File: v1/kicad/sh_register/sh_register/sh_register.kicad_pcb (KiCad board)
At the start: 2 copper layers, 101 x 61.5 mm, 5 parts, among them J1 OP_{out}, U1 74LS194, U2 74LS194, U3 74LS245, U4 LNCPU Type B Connector

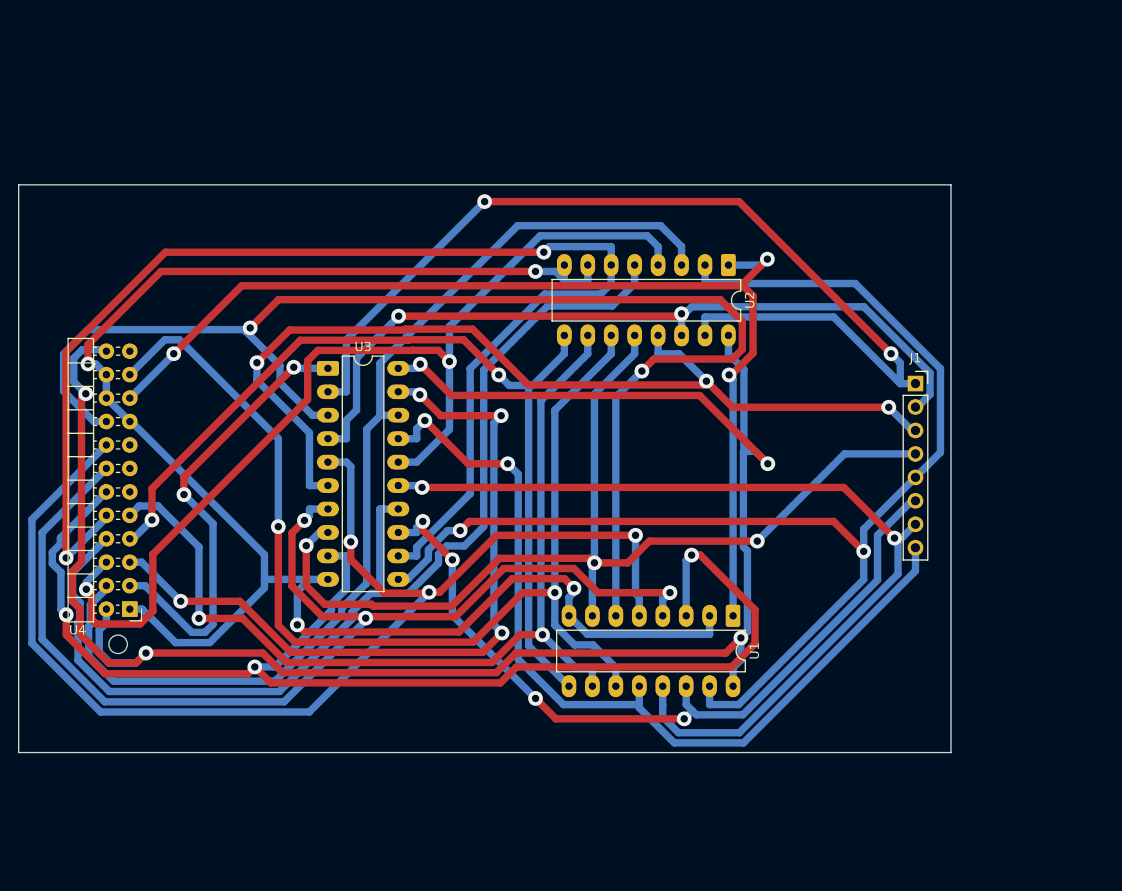
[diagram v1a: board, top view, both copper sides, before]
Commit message: check designs for ALU (partial), SP, Shift register, register
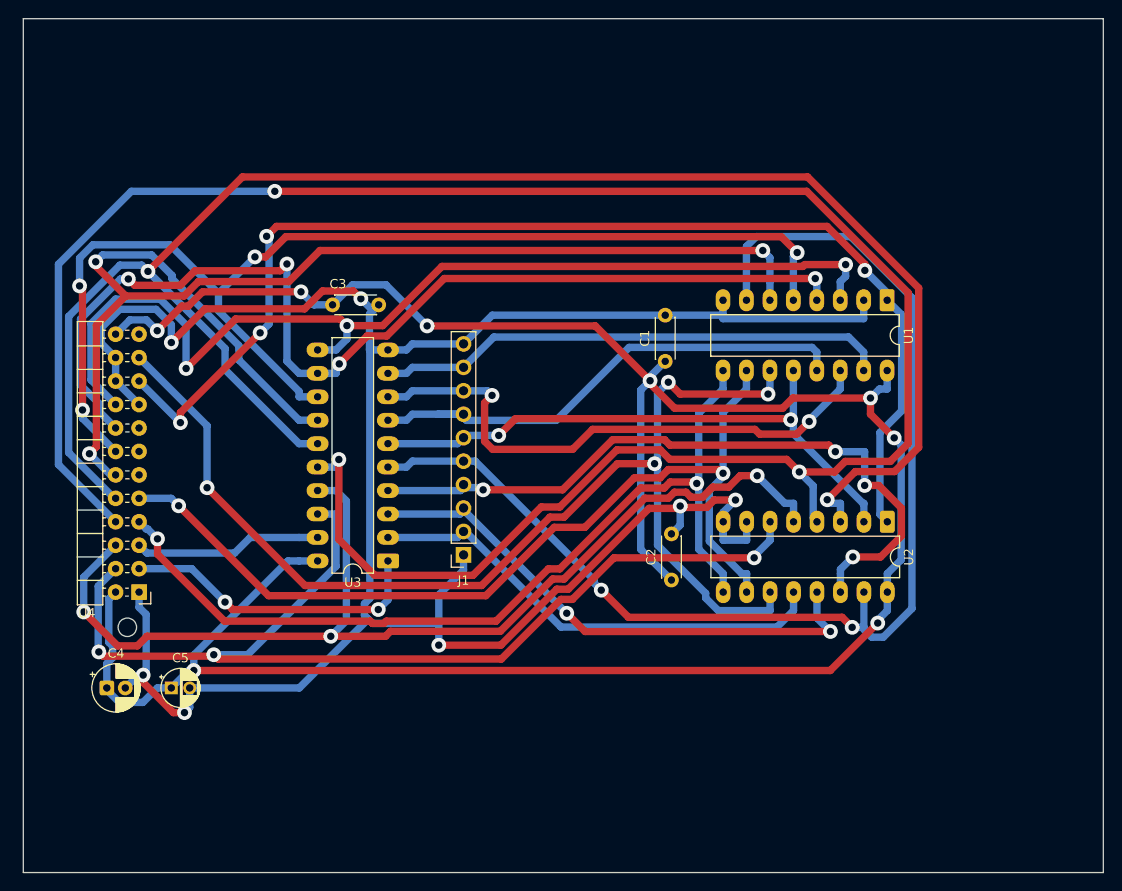
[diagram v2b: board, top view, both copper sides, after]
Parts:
- added C1: 100n, Capacitor_THT:C_Disc_D4.3mm_W1.9mm_P5.00mm, F.Cu at (132.0, 65.6)
- added C2: 100n, Capacitor_THT:C_Disc_D4.3mm_W1.9mm_P5.00mm, F.Cu at (132.7, 89.3)
- added C3: 220n, Capacitor_THT:C_Disc_D4.3mm_W1.9mm_P5.00mm, F.Cu at (96.0, 59.5)
- added C4: 47uF, Capacitor_THT:CP_Radial_D5.0mm_P2.00mm, F.Cu at (71.5, 101.0)
- added C5: 1uF, lncpu:CP_Radial_D4.0mm_P2.00mm-Large-Holes, F.Cu at (78.5, 101.0)
- J1: footprint Connector_PinSocket_2.54mm:PinSocket_1x08_P2.54mm_Vertical -> Connector_PinSocket_2.54mm:PinSocket_1x10_P2.54mm_Vertical
- U3: value 74LS245 -> 74HCT541
- U4: value LNCPU Type B Connector -> LNCPU Type B Header
- moved J1 52.4 mm to (110.2, 86.6), turned to 180 degrees
- moved U1 38.0 mm to (156.1, 59.0)
- moved U2 32.7 mm to (156.1, 83.0)
- moved U3 21.8 mm to (102.0, 87.2), turned to 180 degrees
- moved U4 2.10 mm to (75.0, 90.6)
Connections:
- J1 pad 1: /ASYNC_{out}0 -> Net-(U1-Dsr)
- J1 pad 2: /ASYNC_{out}1 -> /ASYNC_{out}0
- J1 pad 3: /ASYNC_{out}2 -> /ASYNC_{out}1
- J1 pad 4: /ASYNC_{out}3 -> /ASYNC_{out}2
- J1 pad 5: /ASYNC_{out}4 -> /ASYNC_{out}3
- J1 pad 6: /ASYNC_{out}5 -> /ASYNC_{out}4
- J1 pad 7: /ASYNC_{out}6 -> /ASYNC_{out}5
- J1 pad 8: /ASYNC_{out}7 -> /ASYNC_{out}6
- U1 pad 12: /ASYNC_{out}7 -> /ASYNC_{out}4
- U1 pad 13: /ASYNC_{out}6 -> /ASYNC_{out}5
- U1 pad 14: /ASYNC_{out}5 -> /ASYNC_{out}6
- U1 pad 15: /ASYNC_{out}4 -> /ASYNC_{out}7
- U1 pad 3: /DBUS4 -> /DBUS7
- U1 pad 4: /DBUS5 -> /DBUS6
- U1 pad 5: /DBUS6 -> /DBUS5
- U1 pad 6: /DBUS7 -> /DBUS4
- U2 pad 12: /ASYNC_{out}3 -> /ASYNC_{out}0
- U2 pad 13: /ASYNC_{out}2 -> /ASYNC_{out}1
- U2 pad 14: /ASYNC_{out}1 -> /ASYNC_{out}2
- U2 pad 15: /ASYNC_{out}0 -> /ASYNC_{out}3
- U2 pad 3: /DBUS0 -> /DBUS3
- U2 pad 4: /DBUS1 -> /DBUS2
- U2 pad 5: /DBUS2 -> /DBUS1
- U2 pad 6: /DBUS3 -> /DBUS0
- U3 pad 11: /ASYNC_{out}4 -> /DBUS7
- U3 pad 12: /DBUS3 -> /DBUS6
- U3 pad 13: /ASYNC_{out}5 -> /DBUS5
- U3 pad 14: /DBUS2 -> /DBUS4
- U3 pad 15: /ASYNC_{out}6 -> /DBUS3
- U3 pad 16: /DBUS1 -> /DBUS2
- U3 pad 17: /ASYNC_{out}7 -> /DBUS1
- U3 pad 3: /DBUS7 -> /ASYNC_{out}1
- U3 pad 4: /ASYNC_{out}1 -> /ASYNC_{out}2
- U3 pad 5: /DBUS6 -> /ASYNC_{out}3
- U3 pad 6: /ASYNC_{out}2 -> /ASYNC_{out}4
- U3 pad 7: /DBUS5 -> /ASYNC_{out}5
- U3 pad 8: /ASYNC_{out}3 -> /ASYNC_{out}6
- U3 pad 9: /DBUS4 -> /ASYNC_{out}7
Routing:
- net /DBUS2: track 119.2 -> 235.7 mm, vias 0 -> 3
- net Net-(U1-Dsr): track 181.8 -> 254.4 mm, vias 4 -> 7
- net /ASYNC_{out}4: track 136.8 -> 64.7 mm
- net Net-(U3-2OE): track 82.5 -> 20.4 mm, vias 4 -> 0
- net /ASYNC_{out}0: track 111.1 -> 51.2 mm, vias 2 -> 0
- net Net-(U1-VCC): track 209.5 -> 267.8 mm, vias 5 -> 8
- net /DBUS3: track 140.3 -> 186.3 mm
- net /ASYNC_{out}7: track 96.1 -> 55.8 mm, vias 2 -> 0
- net /ASYNC_{out}6: track 99.5 -> 61.2 mm
- net /ASYNC_{out}5: track 85.7 -> 55.3 mm, vias 4 -> 0
- net /DBUS7: track 143.4 -> 113.1 mm, vias 2 -> 3
- net /ASYNC_{out}1: track 85.5 -> 58.7 mm
- net /ASYNC_{out}2: track 103.9 -> 77.2 mm, vias 3 -> 4
- net /DBUS6: track 132.9 -> 114.2 mm, vias 3 -> 4
- net /ASYNC_{out}3: track 113.7 -> 131.8 mm, vias 3 -> 2
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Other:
- board size 101 x 61.5 mm -> 117 x 92.5 mm

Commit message: readapt designs for BR, SP, SR, ALU
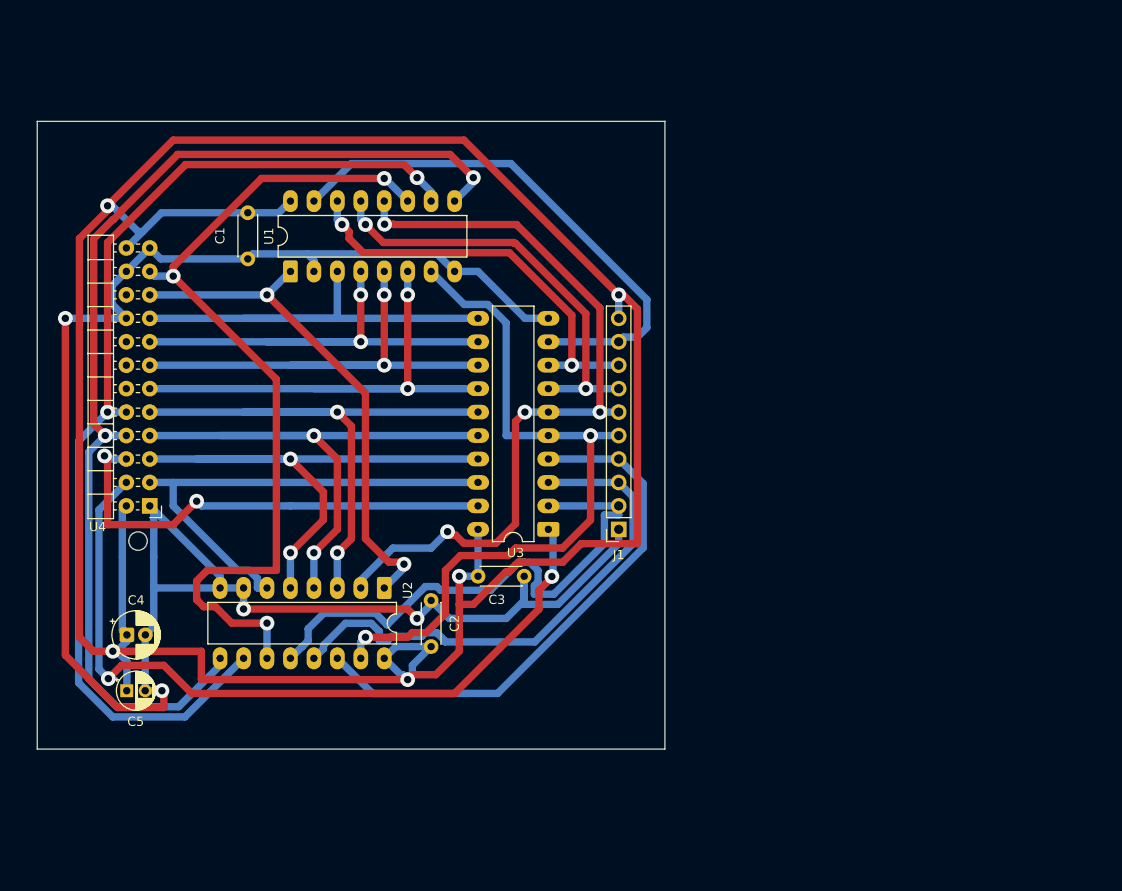
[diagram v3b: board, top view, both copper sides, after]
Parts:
- moved U1 64.7 mm to (91.4, 55.9), turned to 90 degrees
- moved U2 55.0 mm to (101.6, 90.2)
- moved C1 48.0 mm to (86.8, 49.5), turned to -90 degrees
- moved C3 33.4 mm to (111.8, 88.9)
- moved C2 27.0 mm to (106.7, 96.5)
- moved U3 17.7 mm to (119.4, 83.8)
- moved J1 17.0 mm to (127.0, 83.8)
- moved U4 9.41 mm to (76.2, 81.3)
- moved C4 6.15 mm to (73.7, 95.2)
- moved C5 4.83 mm to (73.7, 101.3)
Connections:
- C1 pad 1: Net-(U1-VCC) -> Net-(J1-VCC)
- C2 pad 1: Net-(U1-VCC) -> Net-(J1-VCC)
- C3 pad 1: Net-(U1-VCC) -> Net-(J1-VCC)
- C4 pad 1: Net-(U1-VCC) -> Net-(J1-VCC)
- C5 pad 1: Net-(U1-VCC) -> Net-(J1-VCC)
- J1 pad 10: Net-(U1-Dsr) -> Net-(J1-VCC)
- U1 pad 16: Net-(U1-VCC) -> Net-(J1-VCC)
- U2 pad 16: Net-(U1-VCC) -> Net-(J1-VCC)
- U3 pad 1: Net-(U3-1OE) -> Net-(U3-G1)
- U3 pad 19: Net-(U3-2OE) -> Net-(U3-G2)
- U3 pad 20: Net-(U1-VCC) -> Net-(J1-VCC)
- U4 pad 10: /DBUS3 -> Net-(U1-S1)
- U4 pad 11: unconnected-(U4-CTRL_{4}-Pad11) -> /DBUS4
- U4 pad 12: /DBUS4 -> unconnected-(U4-CTRL_{4}-Pad12)
- U4 pad 13: unconnected-(U4-CTRL_{5}-Pad13) -> /DBUS5
- U4 pad 14: /DBUS5 -> unconnected-(U4-CTRL_{5}-Pad14)
- U4 pad 15: unconnected-(U4-CTRL_{6}-Pad15) -> /DBUS6
- U4 pad 16: /DBUS6 -> unconnected-(U4-CTRL_{6}-Pad16)
- U4 pad 17: Net-(U1-Dsr) -> /DBUS7
- U4 pad 18: /DBUS7 -> Net-(U1-Dsr)
- U4 pad 2: Net-(U1-VCC) -> Net-(J1-VCC)
- U4 pad 20: Net-(U1-Dsr) -> unconnected-(U4-CLK2-Pad20)
- U4 pad 23: unconnected-(U4-CLK2-Pad23) -> Net-(U1-Dsr)
- U4 pad 24: Net-(U1-VCC) -> Net-(J1-VCC)
- U4 pad 3: Net-(U3-1OE) -> /DBUS0
- U4 pad 4: /DBUS0 -> Net-(U3-G1)
- U4 pad 5: Net-(U3-2OE) -> /DBUS1
- U4 pad 6: /DBUS1 -> Net-(U3-G2)
- U4 pad 7: Net-(U1-S0) -> /DBUS2
- U4 pad 8: /DBUS2 -> Net-(U1-S0)
- U4 pad 9: Net-(U1-S1) -> /DBUS3
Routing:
- net Net-(J1-VCC): track 0.00 -> 287.6 mm, vias 0 -> 5
- net Net-(U1-VCC): track 267.8 -> 0.00 mm, vias 8 -> 0
- net /DBUS2: track 235.7 -> 64.3 mm, vias 3 -> 2
- net /DBUS3: track 186.3 -> 66.0 mm
- net Net-(U3-G1): track 0.00 -> 84.9 mm, vias 0 -> 2
- net /DBUS4: track 137.2 -> 58.4 mm, vias 3 -> 2
- net /DBUS5: track 128.5 -> 55.9 mm, vias 4 -> 2
- net Net-(U1-Mr): track 128.4 -> 55.9 mm, vias 4 -> 2
- net /DBUS0: track 115.3 -> 52.5 mm, vias 3 -> 0
- net /DBUS7: track 113.1 -> 50.8 mm, vias 3 -> 0
- net /DBUS6: track 114.2 -> 53.3 mm, vias 4 -> 2
- net /DBUS1: track 117.4 -> 62.6 mm, vias 3 -> 2
- net /ASYNC_{out}3: track 131.8 -> 78.9 mm
- net Net-(U3-G2): track 0.00 -> 51.5 mm, vias 0 -> 2
- net Net-(U1-Dsr): track 254.4 -> 217.2 mm, vias 7 -> 4
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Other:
- board size 117 x 92.5 mm -> 68 x 68 mm
